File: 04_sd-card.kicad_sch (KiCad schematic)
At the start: 10 parts, among them J1 Micro_SD_Card_Det2

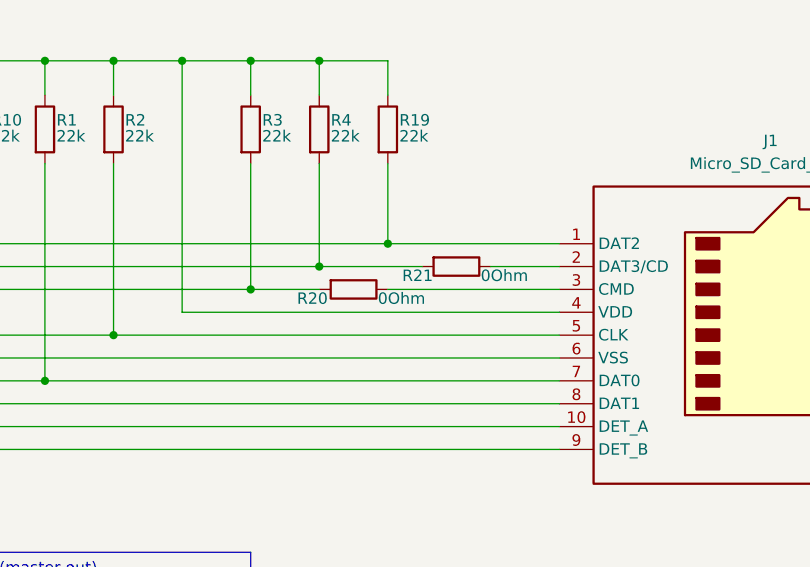
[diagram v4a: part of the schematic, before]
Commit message: v2: major changes
- Move to hierarchical labels
- use another RP Pico Footprint
- split power path in USB/charging and on/off with a button approach in order to control turning on and off
  with the RP Pico, make use of long presses and delay turning of the voltage in order to do a proper shutdown
- introduce another charging controller with a better performance an a lower voltage needed in order to charge the battery
- rework display booster circuit
- rework SD and buttons
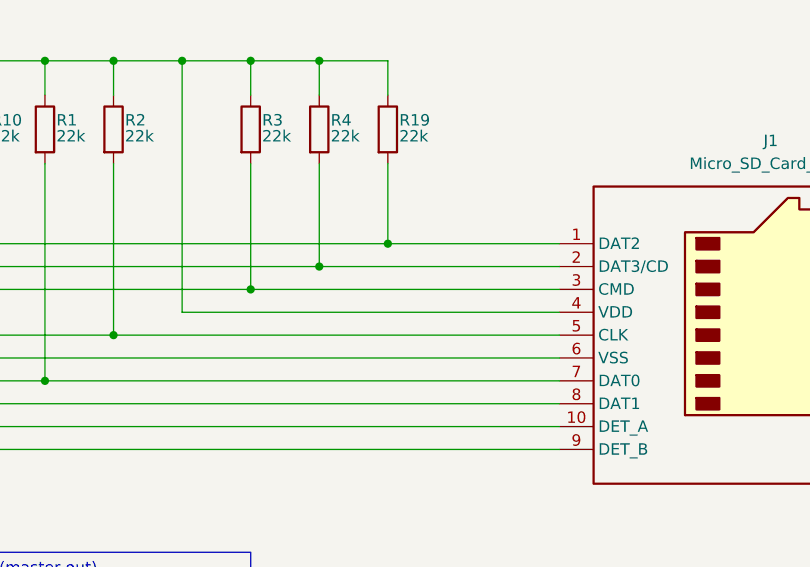
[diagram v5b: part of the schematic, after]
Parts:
- removed R20, R21: 0Ohm, Resistor_SMD:R_1206_3216Metric_Pad1.30x1.75mm_HandSolder, symbol Device:R
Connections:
- net SD_CMD-DI: now also J1.3 (CMD)
- net SD_DAT3-CD-CS: now also J1.2 (DAT3/CD)
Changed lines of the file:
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@@
-	(wire
-		(pts
-			(xy 151.13 90.17) (xy 158.75 90.17)
-		)
-		(stroke
-			(width 0)
-			(type default)
-		)
-	)
 	(wire
 		(pts
@@
 	(wire
 		(pts
-			(xy 139.7 92.71) (xy 158.75 92.71)
-		)
-		(stroke
-			(width 0)
-			(type default)
-		)
-	)
-	(wire
-		(pts
 			(xy 116.84 67.31) (xy 124.46 67.31)
 		)
@@
 	(wire
 		(pts
-			(xy 124.46 92.71) (xy 132.08 92.71)
+			(xy 124.46 92.71) (xy 158.75 92.71)
 		)
 		(stroke
@@
 	(wire
 		(pts
-			(xy 132.08 90.17) (xy 143.51 90.17)
+			(xy 132.08 90.17) (xy 158.75 90.17)
 		)
 		(stroke
@@
 				(path "/ec954637-2a8b-4662-b4a1-f88107f11cb0/5fd074b7-3c47-4717-bcdc-b0d8134ff74e"
 					(reference "R3")
-					(unit 1)
-				)
-			)
-		)
-	)
-	(symbol
-		(lib_id "Device:R")
-		(at 147.32 90.17 270)
-		(unit 1)
-		(exclude_from_sim no)
-		(in_bom yes)
-		(on_board yes)
-		(dnp no)
-		(property "Reference" "R21"
-			(at 143.002 91.186 90)
-			(effects
-				(font
-					(size 1.27 1.27)
-				)
-			)
-		)
-		(property "Value" "0Ohm"
-			(at 152.654 91.186 90)
-			(effects
-				(font
-					(size 1.27 1.27)
-				)
-			)
-		)
-		(property "Footprint" "Resistor_SMD:R_1206_3216Metric_Pad1.30x1.75mm_HandSolder"
-			(at 147.32 88.392 90)
-			(effects
-				(font
-					(size 1.27 1.27)
-				)
-				(hide yes)
-			)
-		)
-		(property "Datasheet" "~"
-			(at 147.32 90.17 0)
-			(effects
-				(font
-					(size 1.27 1.27)
-				)
-				(hide yes)
-			)
-		)
-		(property "Description" "Resistor"
-			(at 147.32 90.17 0)
-			(effects
-				(font
-					(size 1.27 1.27)
-				)
-				(hide yes)
-			)
-		)
-		(pin "2"
-		)
-		(pin "1"
-		)
-		(instances
-			(project "ZEReader-Pico"
-				(path "/ec954637-2a8b-4662-b4a1-f88107f11cb0/5fd074b7-3c47-4717-bcdc-b0d8134ff74e"
-					(reference "R21")
 					(unit 1)
 				)
@@
 					(unit 1)
 				)
-			)
-		)
-	)
-	(symbol
-		(lib_id "Device:R")
-		(at 135.89 92.71 270)
-		(unit 1)
-		(exclude_from_sim no)
-		(in_bom yes)
-		(on_board yes)
-		(dnp no)
-		(property "Reference" "R20"
-			(at 131.318 93.726 90)
-			(effects
-				(font
-					(size 1.27 1.27)
-				)
-			)
-		)
-		(property "Value" "0Ohm"
-			(at 141.224 93.726 90)
-			(effects
-				(font
-					(size 1.27 1.27)
-				)
-			)
-		)
-		(property "Footprint" "Resistor_SMD:R_1206_3216Metric_Pad1.30x1.75mm_HandSolder"
-			(at 135.89 90.932 90)
-			(effects
-				(font
-					(size 1.27 1.27)
-				)
-				(hide yes)
-			)
-		)
-		(property "Datasheet" "~"
-			(at 135.89 92.71 0)
-			(effects
-				(font
-					(size 1.27 1.27)
-				)
-				(hide yes)
-			)
-		)
-		(property "Description" "Resistor"
-			(at 135.89 92.71 0)
-			(effects
-				(font
-					(size 1.27 1.27)
-				)
-				(hide yes)
-			)
-		)
-		(pin "2"
-		)
-		(pin "1"
-		)
-		(instances
-			(project ""
-				(path "/ec954637-2a8b-4662-b4a1-f88107f11cb0/5fd074b7-3c47-4717-bcdc-b0d8134ff74e"
-					(reference "R20")
-					(unit 1)
-				)

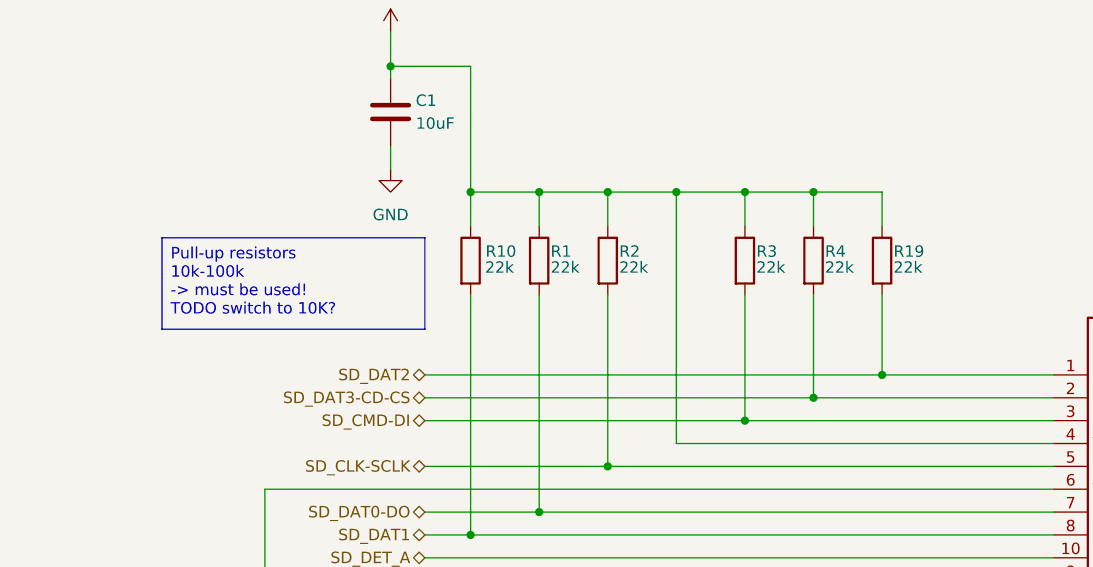
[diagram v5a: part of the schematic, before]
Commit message: v2: finished schematics, start routing
The schematics for v2 should be mostly finished by now.
The new on/off button is ready and tested with a breadboard setup.
It now uses two FETs for a self-holding circuit for turning the
device on and off. To reach a safe logic level for Pico 2, a
2.7V Zener diode is used together with a pull-down for E9 affected
RP2350 revisions.
Besides, most pull-up resistors are 10k now to keep the BoM
smaller.

Routing started with a major redesign.
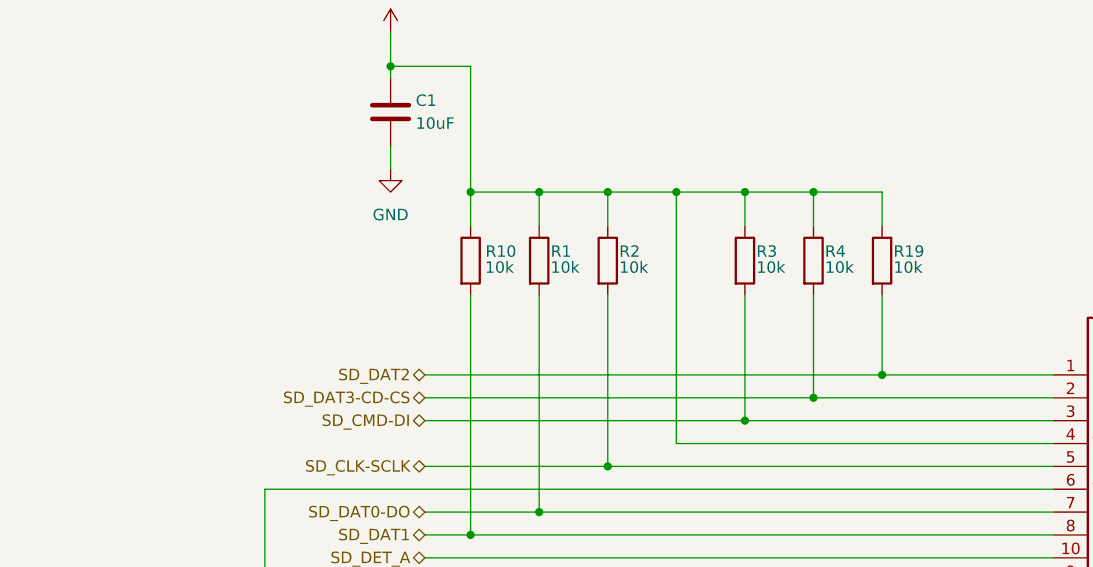
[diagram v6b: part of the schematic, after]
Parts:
- R1, R10, R19, R2, R3, R4: value 22k -> 10k
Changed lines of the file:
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@@
-		)
-	)
-	(text_box "Pull-up resistors\n10k-100k\n-> must be used!\nTODO switch to 10K?"
-		(exclude_from_sim no)
-		(at 59.69 72.39 0)
-		(size 29.21 10.16)
-		(margins 0.9525 0.9525 0.9525 0.9525)
-		(stroke
-			(width 0)
-			(type solid)
-		)
-		(fill
-			(type none)
-		)
-		(effects
-			(font
-				(size 1.27 1.27)
-			)
-			(justify left top)
 		)
 	)
@@
 			)
 		)
-		(property "Value" "22k"
+		(property "Value" "10k"
 			(at 133.35 75.692 0)
 			(effects
@@
 			)
 		)
-		(property "Value" "22k"
+		(property "Value" "10k"
 			(at 98.806 75.692 0)
 			(effects
@@
 			)
 		)
-		(property "Value" "22k"
+		(property "Value" "10k"
 			(at 125.73 75.692 0)
 			(effects
@@
 			)
 		)
-		(property "Value" "22k"
+		(property "Value" "10k"
 			(at 110.49 75.692 0)
 			(effects
@@
 			)
 		)
-		(property "Value" "22k"
+		(property "Value" "10k"
 			(at 140.97 75.692 0)
 			(effects
@@
 			)
 		)
-		(property "Value" "22k"
+		(property "Value" "10k"
 			(at 102.87 75.692 0)
 			(effects

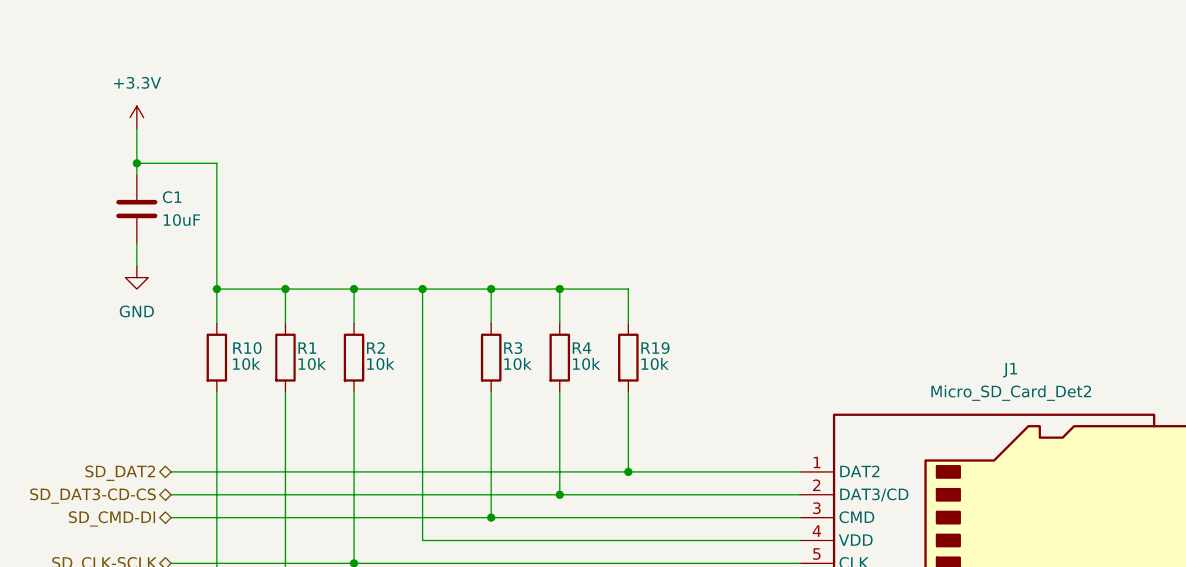
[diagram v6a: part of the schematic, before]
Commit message: Reworked v2 routing
- some general improvements
- reworked component numbering
- routed and tuned differential pair (USB)
- added stiching vias and improved ground fills
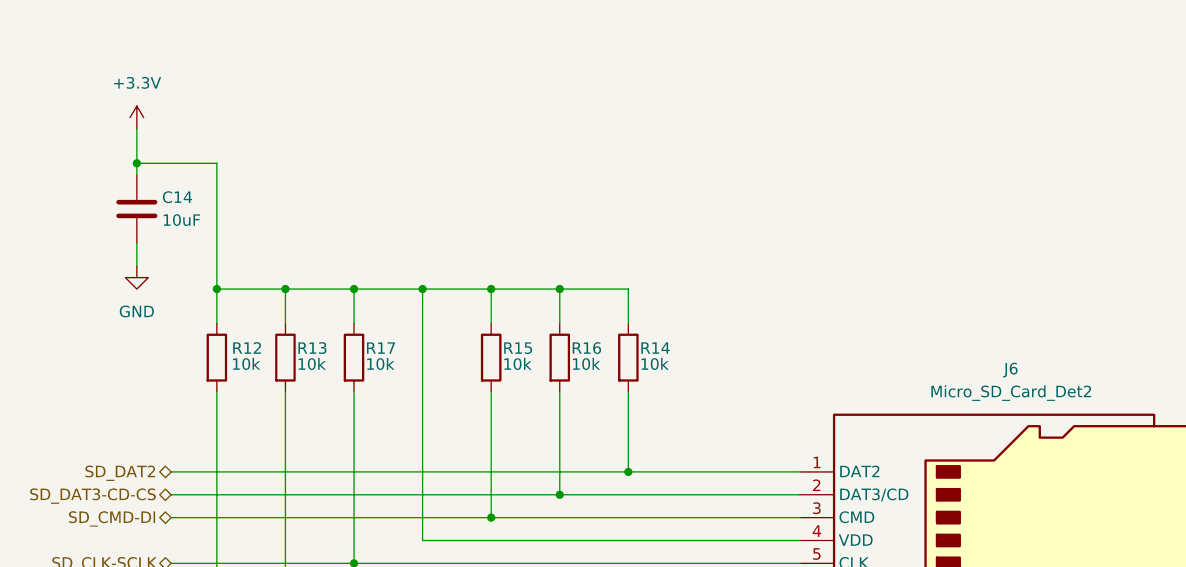
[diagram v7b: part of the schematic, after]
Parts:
- renumbered C1 to C14, J1 to J6, R10 to R12, R1 to R13, R19 to R14, R3 to R15, R4 to R16, R2 to R17
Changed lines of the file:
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@@
 		(on_board yes)
 		(dnp no)
-		(property "Reference" "R4"
+		(property "Reference" "R16"
 			(at 133.35 73.9139 0)
 			(effects
@@
 			(project "ZEReader-Pico"
 				(path "/ec954637-2a8b-4662-b4a1-f88107f11cb0/5fd074b7-3c47-4717-bcdc-b0d8134ff74e"
-					(reference "R4")
+					(reference "R16")
 					(unit 1)
 				)
@@
 		(on_board yes)
 		(dnp no)
-		(property "Reference" "R10"
+		(property "Reference" "R12"
 			(at 99.06 73.914 0)
 			(effects
@@
 			(project "ZEReader-Pico"
 				(path "/ec954637-2a8b-4662-b4a1-f88107f11cb0/5fd074b7-3c47-4717-bcdc-b0d8134ff74e"
-					(reference "R10")
+					(reference "R12")
 					(unit 1)
 				)
@@
 		(on_board yes)
 		(dnp no)
-		(property "Reference" "R3"
+		(property "Reference" "R15"
 			(at 125.73 73.9139 0)
 			(effects
@@
 			(project "ZEReader-Pico"
 				(path "/ec954637-2a8b-4662-b4a1-f88107f11cb0/5fd074b7-3c47-4717-bcdc-b0d8134ff74e"
-					(reference "R3")
+					(reference "R15")
 					(unit 1)
 				)
@@
 		(on_board yes)
 		(dnp no)
-		(property "Reference" "C1"
+		(property "Reference" "C14"
 			(at 87.884 57.15 0)
 			(effects
@@
 			(project ""
 				(path "/ec954637-2a8b-4662-b4a1-f88107f11cb0/5fd074b7-3c47-4717-bcdc-b0d8134ff74e"
-					(reference "C1")
+					(reference "C14")
 					(unit 1)
 				)
@@
 		(on_board yes)
 		(dnp no)
-		(property "Reference" "R2"
+		(property "Reference" "R17"
 			(at 110.49 73.9139 0)
 			(effects
@@
 			(project "ZEReader-Pico"
 				(path "/ec954637-2a8b-4662-b4a1-f88107f11cb0/5fd074b7-3c47-4717-bcdc-b0d8134ff74e"
-					(reference "R2")
+					(reference "R17")
 					(unit 1)
 				)
@@
 		(on_board yes)
 		(dnp no)
-		(property "Reference" "R19"
+		(property "Reference" "R14"
 			(at 140.97 73.9139 0)
 			(effects
@@
 			(project "ZEReader-Pico"
 				(path "/ec954637-2a8b-4662-b4a1-f88107f11cb0/5fd074b7-3c47-4717-bcdc-b0d8134ff74e"
-					(reference "R19")
+					(reference "R14")
 					(unit 1)
 				)
@@
 		(on_board yes)
 		(dnp no)
-		(property "Reference" "R1"
+		(property "Reference" "R13"
 			(at 102.87 73.914 0)
 			(effects
@@
 			(project ""
 				(path "/ec954637-2a8b-4662-b4a1-f88107f11cb0/5fd074b7-3c47-4717-bcdc-b0d8134ff74e"
-					(reference "R1")
+					(reference "R13")
 					(unit 1)
 				)
@@
 		(dnp no)
 		(fields_autoplaced yes)
-		(property "Reference" "J1"
+		(property "Reference" "J6"
 			(at 182.245 76.2 0)
 			(effects
@@
 			(project ""
 				(path "/ec954637-2a8b-4662-b4a1-f88107f11cb0/5fd074b7-3c47-4717-bcdc-b0d8134ff74e"
-					(reference "J1")
-					(unit 1)
-				)
+					(reference "J6")
+					(unit 1)
+				)
